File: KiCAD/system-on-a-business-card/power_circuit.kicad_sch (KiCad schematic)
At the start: 10 parts, among them U4 ZD1117ILTRAD

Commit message: minor tweaks in design, added thermal relief vias
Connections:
- net GND: now also U4.4 (GND)
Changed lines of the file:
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@@
   (junction (at 118.11 52.07) (diameter 0) (color 0 0 0 0)
+  )
+  (junction (at 124.46 81.28) (diameter 0) (color 0 0 0 0)
   )
   (junction (at 106.68 52.07) (diameter 0) (color 0 0 0 0)
@@
     (stroke (width 0) (type default) (color 0 0 0 0))
   )
+  (wire (pts (xy 124.46 81.28) (xy 128.27 81.28))
+    (stroke (width 0) (type default) (color 0 0 0 0))
+  )
   (wire (pts (xy 118.11 52.07) (xy 119.38 52.07))
     (stroke (width 0) (type default) (color 0 0 0 0))
   )
   (wire (pts (xy 85.09 63.5) (xy 85.09 81.28))
+    (stroke (width 0) (type default) (color 0 0 0 0))
+  )
+  (wire (pts (xy 124.46 63.5) (xy 124.46 81.28))
     (stroke (width 0) (type default) (color 0 0 0 0))
   )
@@
     (stroke (width 0) (type default) (color 0 0 0 0))
   )
-  (wire (pts (xy 113.03 81.28) (xy 128.27 81.28))
+  (wire (pts (xy 113.03 81.28) (xy 124.46 81.28))
     (stroke (width 0) (type default) (color 0 0 0 0))
   )

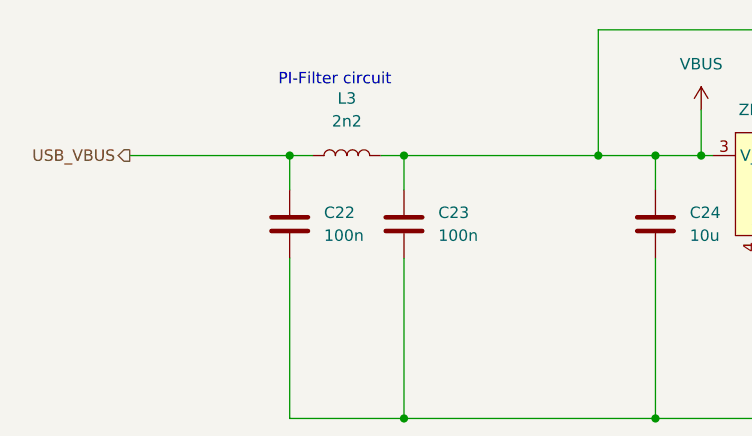
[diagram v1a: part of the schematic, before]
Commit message: fixed #12 connected OLED VDD pins to 3.3V power line
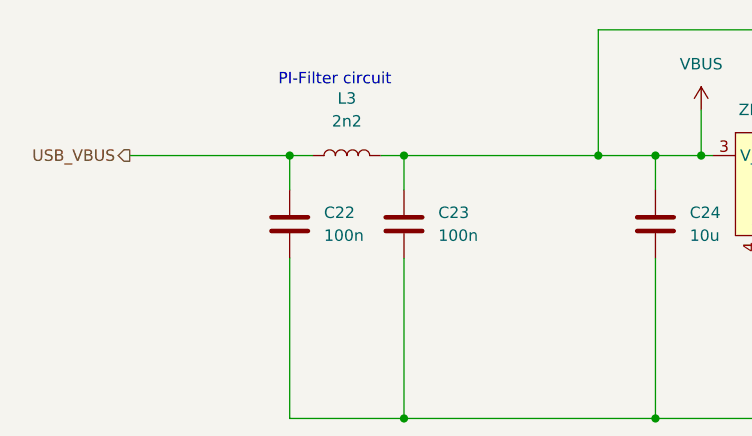
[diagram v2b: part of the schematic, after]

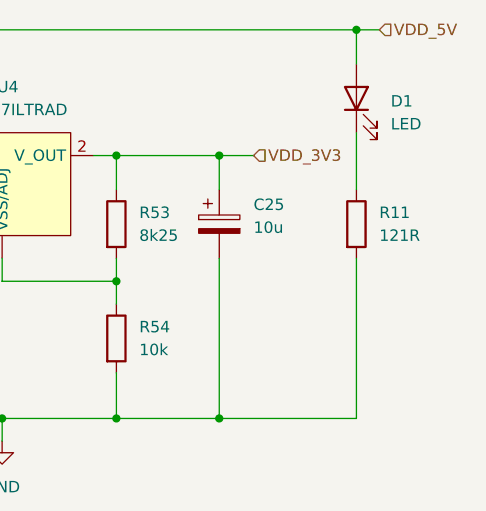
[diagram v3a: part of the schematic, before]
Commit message: resolves #13: changed resistor for LED from 121R to 47k to reduce brightness significantly
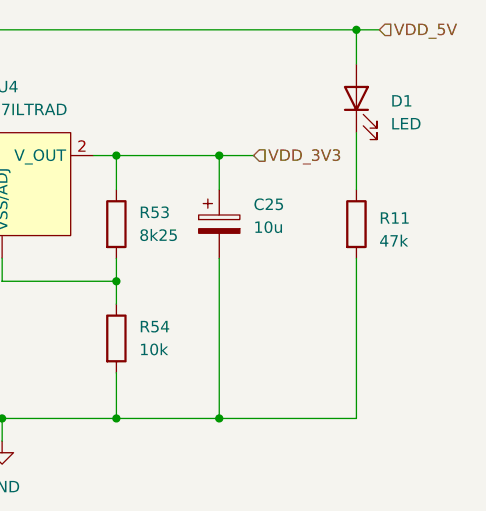
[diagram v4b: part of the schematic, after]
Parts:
- R11: value 121R -> 47k
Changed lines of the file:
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@@
   (symbol (lib_id "Device:R") (at 167.64 59.69 0) (unit 1)
     (in_bom yes) (on_board yes) (dnp no) (fields_autoplaced)
-    (property "Reference" "R11" (at 170.18 58.4199 0)
+    (property "Reference" "R11" (at 170.18 59.055 0)
       (effects (font (size 1.27 1.27)) (justify left))
     )
-    (property "Value" "121R" (at 170.18 60.9599 0)
+    (property "Value" "47k" (at 170.18 61.595 0)
       (effects (font (size 1.27 1.27)) (justify left))
     )

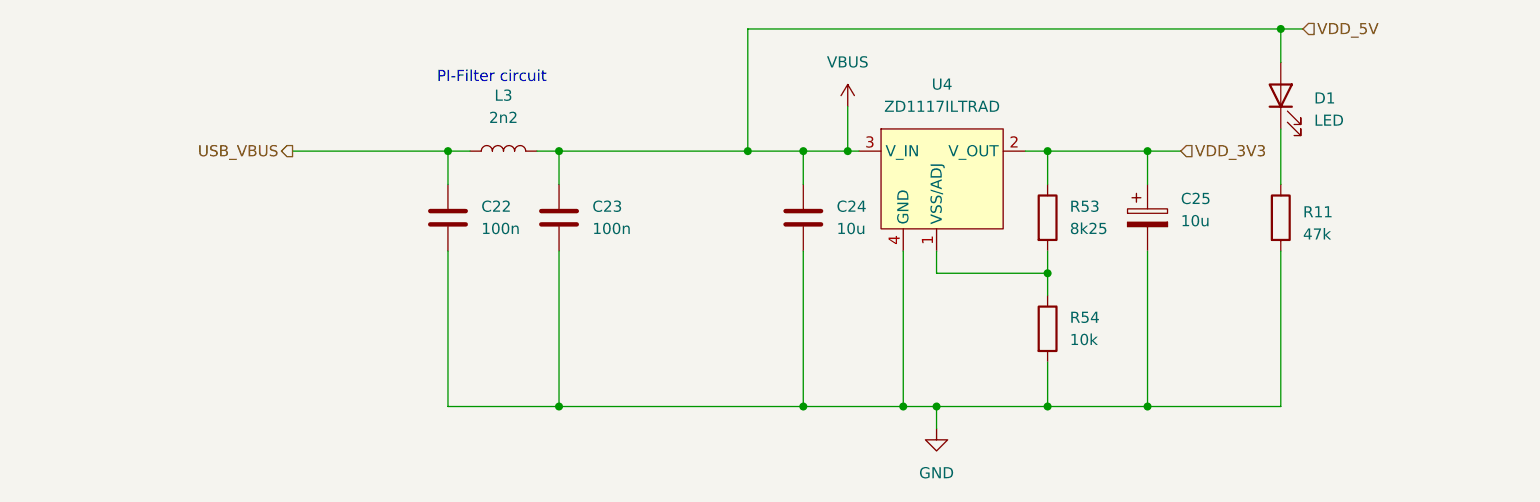
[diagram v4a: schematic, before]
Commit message: fixes #17: updates resistor values R53 and R54, updated board revision silkscreen
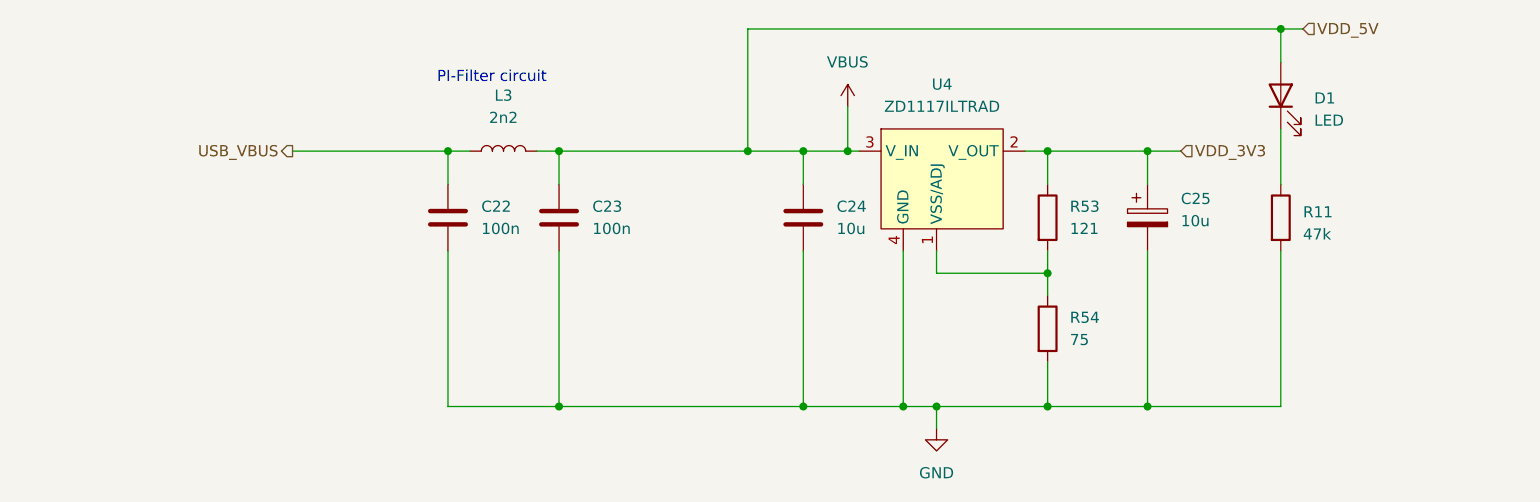
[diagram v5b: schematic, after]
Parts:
- R53: value 8k25 -> 121
- R54: value 10k -> 75
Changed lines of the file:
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@@
       (effects (font (size 1.27 1.27)) (justify left))
     )
-    (property "Value" "10k" (at 143.51 73.6599 0)
+    (property "Value" "75" (at 143.51 73.6599 0)
       (effects (font (size 1.27 1.27)) (justify left))
     )
@@
       (effects (font (size 1.27 1.27)) (justify left))
     )
-    (property "Value" "8k25" (at 143.51 60.9599 0)
+    (property "Value" "121" (at 143.51 60.9599 0)
       (effects (font (size 1.27 1.27)) (justify left))
     )

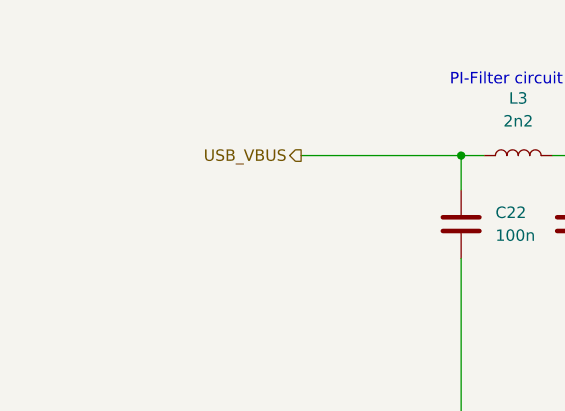
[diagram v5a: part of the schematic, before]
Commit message: #10: added buzzer, io-expander, removed transistors from resistive pad cirucit
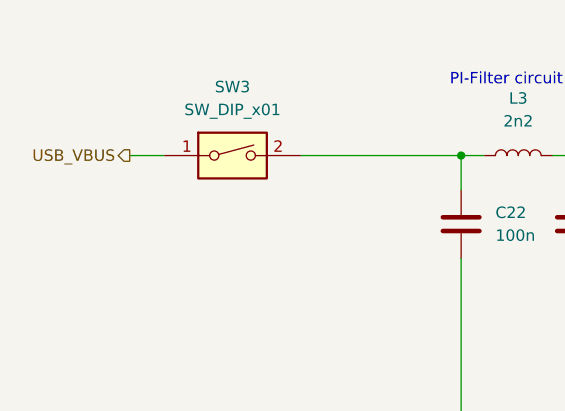
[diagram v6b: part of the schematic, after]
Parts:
- added SW3: SW_DIP_x01, symbol Switch:SW_DIP_x01
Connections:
- net USB_VBUS: now also SW3.1; no longer C22.1, L3.1
- new net: C22.1, L3.1, SW3.2
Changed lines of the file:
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@@
+    (stroke (width 0) (type default))
+  )
+  (wire (pts (xy 35.56 52.07) (xy 39.37 52.07))
     (stroke (width 0) (type default))
   )
@@
     (effects (font (size 1.27 1.27)) (justify left))
   )
-  (hierarchical_label "USB_VBUS" (shape output) (at 54.61 52.07 180) (fields_autoplaced)
+  (hierarchical_label "USB_VBUS" (shape output) (at 35.56 52.07 180) (fields_autoplaced)
     (effects (font (size 1.27 1.27)) (justify right))
   )
@@
         )
       )
+    )
+  )
+  (symbol (lib_id "Switch:SW_DIP_x01") (at 46.99 52.07 0) (unit 1)
+    (in_bom yes) (on_board yes) (dnp no) (fields_autoplaced)
+    (property "Reference" "SW3" (at 46.99 44.45 0)
+      (effects (font (size 1.27 1.27)))
+    )
+    (property "Value" "SW_DIP_x01" (at 46.99 46.99 0)
+      (effects (font (size 1.27 1.27)))
+    )
+    (property "Footprint" "" (at 46.99 52.07 0)
+      (effects (font (size 1.27 1.27)) hide)
+    )
+    (property "Datasheet" "~" (at 46.99 52.07 0)
+      (effects (font (size 1.27 1.27)) hide)
+    )
+    (pin "1")
+    (pin "2")
+    (instances
+      (project "system-on-a-business-card"
+        (path "/49855302-2ecc-4f42-8bbd-b9c2e284f529/eba2cd67-fe31-4e76-9673-7c97f7251114"
+          (reference "SW3") (unit 1)
+        )
+      )

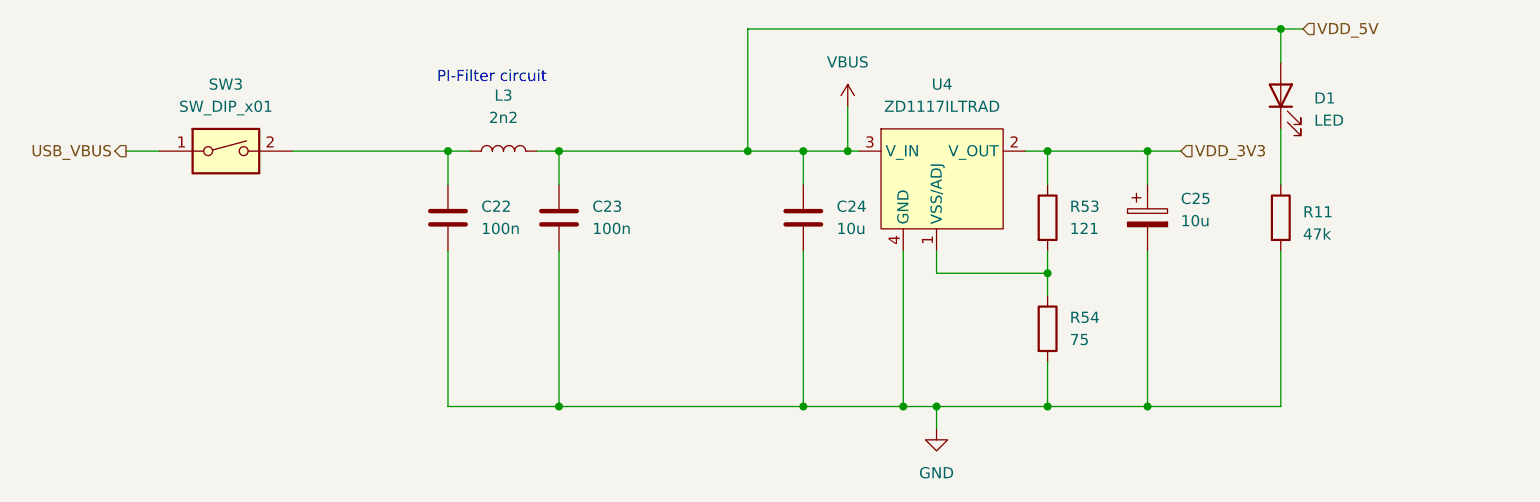
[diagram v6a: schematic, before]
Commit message: #10: added LED for 3.3V rail
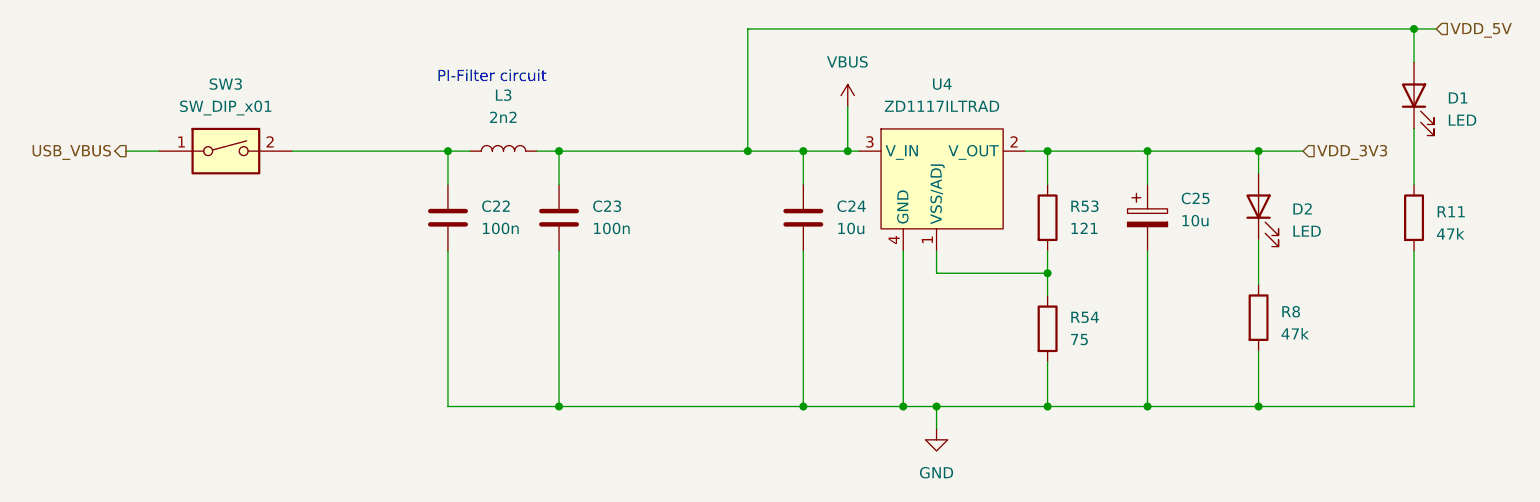
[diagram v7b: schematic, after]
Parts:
- added D2: LED, Diode_SMD:D_0402_1005Metric_Pad0.77x0.64mm_HandSolder, symbol Device:LED
- added R8: 47k, Resistor_SMD:R_0402_1005Metric_Pad0.72x0.64mm_HandSolder, symbol Device:R
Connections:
- net GND: now also R8.2
- net VDD_3V3: now also D2.2 (A)
- new net: D2.1 (K), R8.1
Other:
- moved on the sheet: D1, R11
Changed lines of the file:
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@@
   (junction (at 124.46 81.28) (diameter 0) (color 0 0 0 0)
   )
+  (junction (at 165.1 52.07) (diameter 0) (color 0 0 0 0)
+  )
+  (junction (at 165.1 81.28) (diameter 0) (color 0 0 0 0)
+  )
   (junction (at 106.68 52.07) (diameter 0) (color 0 0 0 0)
   )
@@
   (junction (at 152.4 52.07) (diameter 0) (color 0 0 0 0)
   )
-  (junction (at 167.64 38.1) (diameter 0) (color 0 0 0 0)
+  (junction (at 182.88 38.1) (diameter 0) (color 0 0 0 0)
   )
   (junction (at 113.03 52.07) (diameter 0) (color 0 0 0 0)
@@
     (stroke (width 0) (type default))
   )
-  (wire (pts (xy 167.64 38.1) (xy 106.68 38.1))
+  (wire (pts (xy 165.1 52.07) (xy 170.18 52.07))
     (stroke (width 0) (type default))
   )
@@
     (stroke (width 0) (type default))
   )
-  (wire (pts (xy 167.64 38.1) (xy 170.18 38.1))
-    (stroke (width 0) (type default))
-  )
-  (wire (pts (xy 167.64 41.91) (xy 167.64 38.1))
+  (wire (pts (xy 165.1 62.23) (xy 165.1 67.31))
+    (stroke (width 0) (type default))
+  )
+  (wire (pts (xy 182.88 38.1) (xy 185.42 38.1))
+    (stroke (width 0) (type default))
+  )
+  (wire (pts (xy 182.88 41.91) (xy 182.88 38.1))
+    (stroke (width 0) (type default))
+  )
+  (wire (pts (xy 165.1 81.28) (xy 182.88 81.28))
+    (stroke (width 0) (type default))
+  )
+  (wire (pts (xy 165.1 74.93) (xy 165.1 81.28))
+    (stroke (width 0) (type default))
+  )
+  (wire (pts (xy 106.68 38.1) (xy 182.88 38.1))
     (stroke (width 0) (type default))
   )
@@
     (stroke (width 0) (type default))
   )
-  (wire (pts (xy 152.4 81.28) (xy 167.64 81.28))
+  (wire (pts (xy 152.4 81.28) (xy 165.1 81.28))
     (stroke (width 0) (type default))
   )
@@
     (stroke (width 0) (type default))
   )
-  (wire (pts (xy 167.64 63.5) (xy 167.64 81.28))
+  (wire (pts (xy 182.88 63.5) (xy 182.88 81.28))
     (stroke (width 0) (type default))
   )
@@
     (stroke (width 0) (type default))
   )
-  (wire (pts (xy 167.64 49.53) (xy 167.64 55.88))
+  (wire (pts (xy 182.88 49.53) (xy 182.88 55.88))
     (stroke (width 0) (type default))
   )
@@
     (stroke (width 0) (type default))
   )
-  (wire (pts (xy 152.4 52.07) (xy 156.21 52.07))
+  (wire (pts (xy 152.4 52.07) (xy 165.1 52.07))
     (stroke (width 0) (type default))
   )
@@
   )
   (wire (pts (xy 106.68 38.1) (xy 106.68 52.07))
+    (stroke (width 0) (type default))
+  )
+  (wire (pts (xy 165.1 52.07) (xy 165.1 54.61))
     (stroke (width 0) (type default))
   )
@@
     (effects (font (size 1.27 1.27)) (justify left bottom))
   )
-  (hierarchical_label "VDD_3V3" (shape input) (at 156.21 52.07 0) (fields_autoplaced)
+  (hierarchical_label "VDD_3V3" (shape input) (at 170.18 52.07 0) (fields_autoplaced)
     (effects (font (size 1.27 1.27)) (justify left))
   )
@@
     (effects (font (size 1.27 1.27)) (justify right))
   )
-  (hierarchical_label "VDD_5V" (shape input) (at 170.18 38.1 0) (fields_autoplaced)
+  (hierarchical_label "VDD_5V" (shape input) (at 185.42 38.1 0) (fields_autoplaced)
     (effects (font (size 1.27 1.27)) (justify left))
   )
-  (symbol (lib_id "Device:LED") (at 167.64 45.72 90) (unit 1)
-    (in_bom yes) (on_board yes) (dnp no) (fields_autoplaced)
-    (property "Reference" "D1" (at 171.45 46.0374 90)
+  (symbol (lib_id "Device:LED") (at 182.88 45.72 90) (unit 1)
+    (in_bom yes) (on_board yes) (dnp no) (fields_autoplaced)
+    (property "Reference" "D1" (at 186.69 46.0374 90)
       (effects (font (size 1.27 1.27)) (justify right))
     )
-    (property "Value" "LED" (at 171.45 48.5774 90)
+    (property "Value" "LED" (at 186.69 48.5774 90)
       (effects (font (size 1.27 1.27)) (justify right))
     )
-    (property "Footprint" "Diode_SMD:D_0402_1005Metric_Pad0.77x0.64mm_HandSolder" (at 167.64 45.72 0)
-      (effects (font (size 1.27 1.27)) hide)
-    )
-    (property "Datasheet" "~" (at 167.64 45.72 0)
+    (property "Footprint" "Diode_SMD:D_0402_1005Metric_Pad0.77x0.64mm_HandSolder" (at 182.88 45.72 0)
+      (effects (font (size 1.27 1.27)) hide)
+    )
+    (property "Datasheet" "~" (at 182.88 45.72 0)
       (effects (font (size 1.27 1.27)) hide)
     )
@@
     )
   )
-  (symbol (lib_id "Device:R") (at 167.64 59.69 0) (unit 1)
-    (in_bom yes) (on_board yes) (dnp no) (fields_autoplaced)
-    (property "Reference" "R11" (at 170.18 59.055 0)
-      (effects (font (size 1.27 1.27)) (justify left))
-    )
-    (property "Value" "47k" (at 170.18 61.595 0)
-      (effects (font (size 1.27 1.27)) (justify left))
-    )
-    (property "Footprint" "Resistor_SMD:R_0402_1005Metric_Pad0.72x0.64mm_HandSolder" (at 165.862 59.69 90)
-      (effects (font (size 1.27 1.27)) hide)
-    )
-    (property "Datasheet" "~" (at 167.64 59.69 0)
-      (effects (font (size 1.27 1.27)) hide)
-    )
+  (symbol (lib_id "Device:R") (at 165.1 71.12 0) (unit 1)
+    (in_bom yes) (on_board yes) (dnp no) (fields_autoplaced)
+    (property "Reference" "R8" (at 167.64 70.485 0)
+      (effects (font (size 1.27 1.27)) (justify left))
+    )
+    (property "Value" "47k" (at 167.64 73.025 0)
+      (effects (font (size 1.27 1.27)) (justify left))
+    )
+    (property "Footprint" "Resistor_SMD:R_0402_1005Metric_Pad0.72x0.64mm_HandSolder" (at 163.322 71.12 90)
+      (effects (font (size 1.27 1.27)) hide)
+    )
+    (property "Datasheet" "~" (at 165.1 71.12 0)
+      (effects (font (size 1.27 1.27)) hide)
+    )
+    (pin "1")
+    (pin "2")
+    (instances
+      (project "system-on-a-business-card"
+        (path "/49855302-2ecc-4f42-8bbd-b9c2e284f529/eba2cd67-fe31-4e76-9673-7c97f7251114"
+          (reference "R8") (unit 1)
+        )
+      )
+    )
+  )
+  (symbol (lib_id "Device:LED") (at 165.1 58.42 90) (unit 1)
+    (in_bom yes) (on_board yes) (dnp no) (fields_autoplaced)
+    (property "Reference" "D2" (at 168.91 58.7374 90)
+      (effects (font (size 1.27 1.27)) (justify right))
+    )
+    (property "Value" "LED" (at 168.91 61.2774 90)
+      (effects (font (size 1.27 1.27)) (justify right))
+    )
+    (property "Footprint" "Diode_SMD:D_0402_1005Metric_Pad0.77x0.64mm_HandSolder" (at 165.1 58.42 0)
+      (effects (font (size 1.27 1.27)) hide)
+    )
+    (property "Datasheet" "~" (at 165.1 58.42 0)
+      (effects (font (size 1.27 1.27)) hide)
+    )
+    (pin "1")
+    (pin "2")
+    (instances
+      (project "system-on-a-business-card"
+        (path "/49855302-2ecc-4f42-8bbd-b9c2e284f529/eba2cd67-fe31-4e76-9673-7c97f7251114"
+          (reference "D2") (unit 1)
+        )
+      )
+    )
+  )
+  (symbol (lib_id "Device:R") (at 182.88 59.69 0) (unit 1)
+    (in_bom yes) (on_board yes) (dnp no) (fields_autoplaced)
+    (property "Reference" "R11" (at 185.42 59.055 0)
+      (effects (font (size 1.27 1.27)) (justify left))
+    )
+    (property "Value" "47k" (at 185.42 61.595 0)
+      (effects (font (size 1.27 1.27)) (justify left))
+    )
+    (property "Footprint" "Resistor_SMD:R_0402_1005Metric_Pad0.72x0.64mm_HandSolder" (at 181.102 59.69 90)
+      (effects (font (size 1.27 1.27)) hide)
+    )
+    (property "Datasheet" "~" (at 182.88 59.69 0)
+      (effects (font (size 1.27 1.27)) hide)
+    )
